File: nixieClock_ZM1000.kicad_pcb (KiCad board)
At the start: 2 copper layers, 124.5 x 88.5 mm, 66 parts, among them J1 Conn_01x08_Female, J2 Conn_01x02_Female, Q1 BC547, Q2 BC547, Q3 BC547, Q4 BC547, Q5 BC547, Q6 BC547, Q7 Q_NMOS_GDS, T1 Transformer_1P_1S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

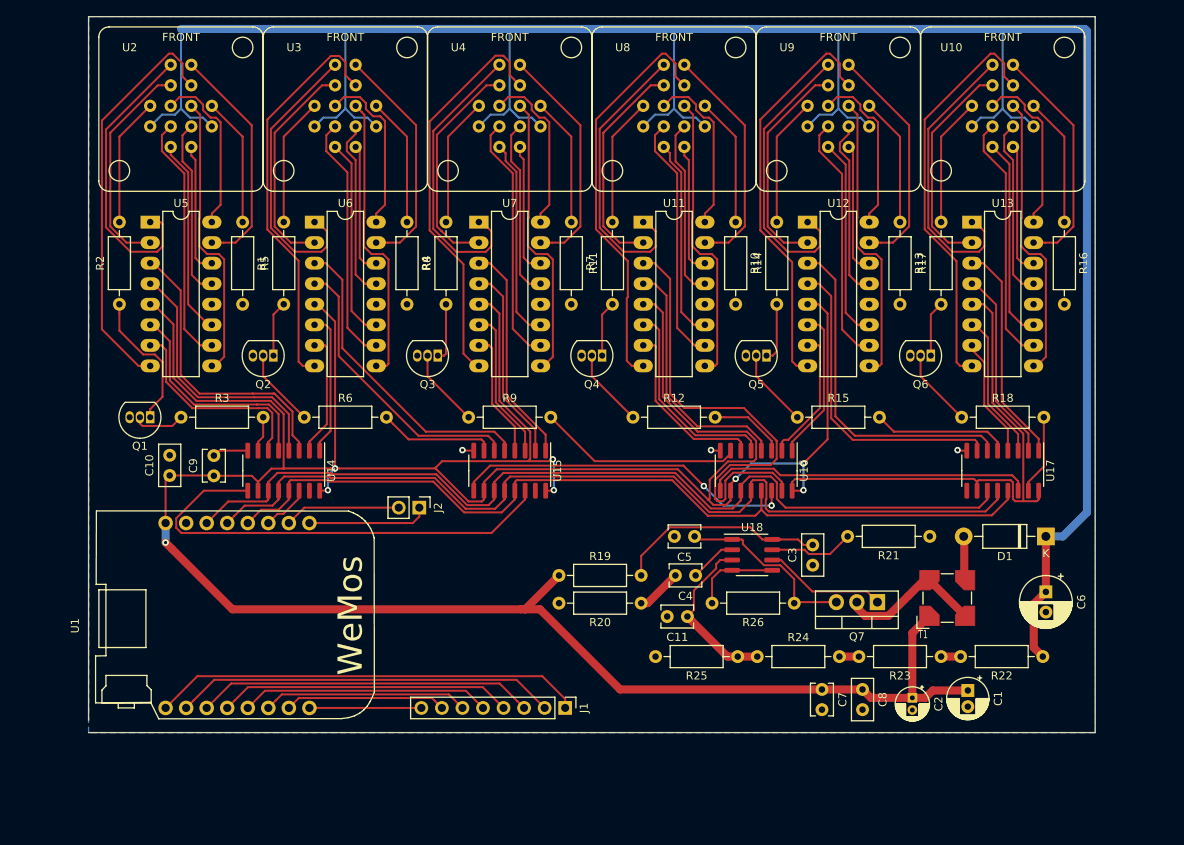
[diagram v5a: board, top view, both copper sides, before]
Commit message: Szitched to DIP shift registers, added BME280
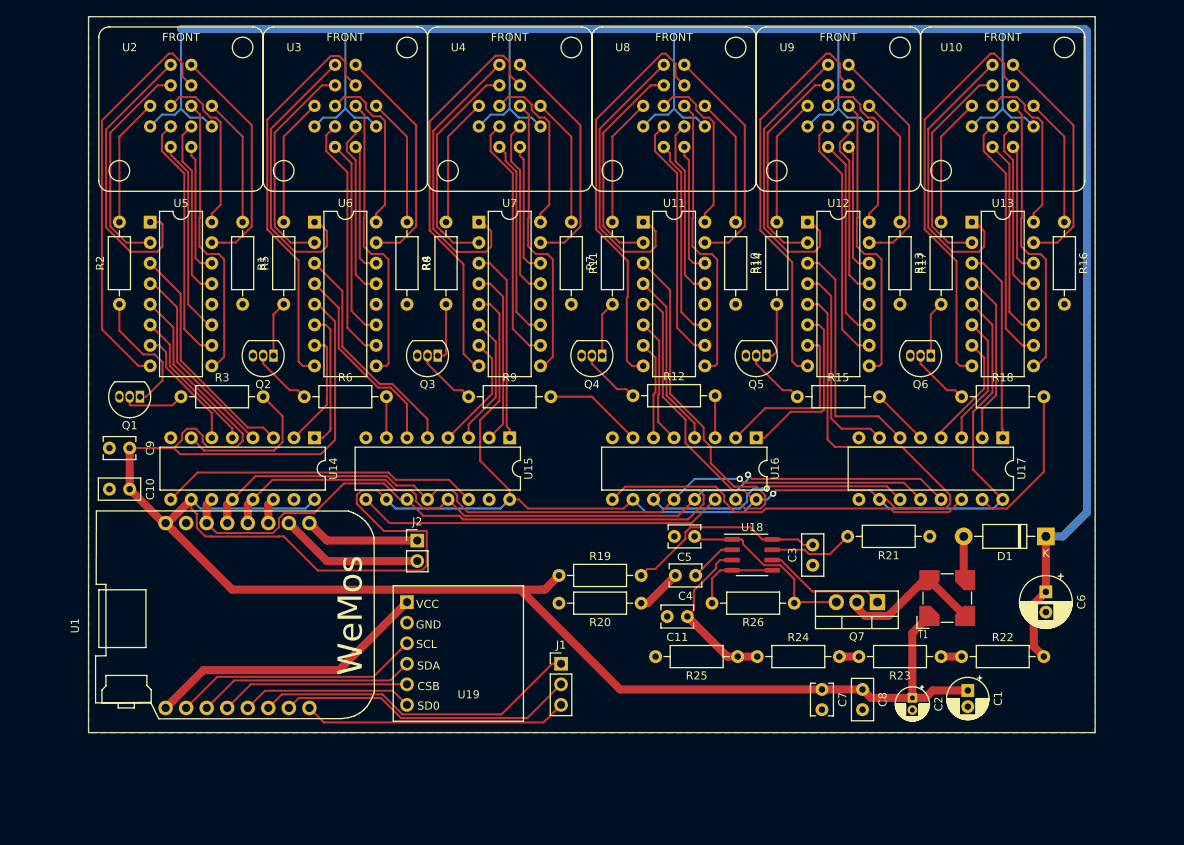
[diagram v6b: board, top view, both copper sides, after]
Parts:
- added U19: BME280, nixies:BME280, F.Cu at (123.2, 125.7)
- J1: value Conn_01x08_Female -> Conn_01x03_Female; footprint Connector_PinHeader_2.54mm:PinHeader_1x08_P2.54mm_Vertical -> Connector_PinHeader_2.54mm:PinHeader_1x03_P2.54mm_Vertical
- U11, U12, U13, U5, U6, U7: footprint Package_DIP:DIP-16_W7.62mm_LongPads -> Package_DIP:DIP-16_W7.62mm
- U14, U15, U16, U17: footprint Package_SO:SOIC-16_3.9x9.9mm_P1.27mm -> Package_DIP:DIP-16_W7.62mm
- moved C9 11.0 mm to (82.5, 100.3), turned to 180 degrees
- moved R22 10.0 mm to (185.4, 126.1), turned to 0 degrees
- moved U14 5.57 mm to (105.4, 99.1)
- moved J1 5.48 mm to (135.9, 127.0), turned to 0 degrees
- moved C10 5.23 mm to (82.5, 105.4), turned to 180 degrees
- moved J2 4.07 mm to (118.1, 111.8), turned to 0 degrees
- moved U15 4.06 mm to (129.5, 99.1)
- moved U16 4.06 mm to (160.0, 99.1)
- moved U17 4.06 mm to (190.5, 99.1)
- moved Q1 2.84 mm to (83.8, 94.0)
- moved R12 2.67 mm to (144.8, 93.9)
- moved R15 2.54 mm to (165.1, 94.0)
- moved R18 2.54 mm to (185.4, 94.0)
- moved R3 2.54 mm to (88.9, 94.0)
- moved R6 2.54 mm to (104.1, 94.0)
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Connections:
- U1 pad 10: Net-(J1-Pad7) -> Net-(J1-Pad2)
- U1 pad 11: Net-(J1-Pad6) -> Net-(J1-Pad1)
- U1 pad 12: Net-(J1-Pad5) -> Net-(U1-Pad12)
- U1 pad 13: Net-(J1-Pad4) -> Net-(U1-Pad13)
- U1 pad 14: Net-(J1-Pad3) -> Net-(U1-Pad14)
- U1 pad 15: Net-(J1-Pad2) -> Net-(U1-Pad15)
- U1 pad 16: Net-(J1-Pad1) -> Net-(U1-Pad16)
- U1 pad 9: Net-(J1-Pad8) -> Net-(J1-Pad3)
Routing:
- net /Control/5V: track 456.2 -> 505.5 mm, vias 8 -> 1
- net Net-(J1-Pad4): track 36.3 -> 0.00 mm
- net Net-(U1-Pad16): track 0.00 -> 35.3 mm
- net Net-(J1-Pad5): track 30.8 -> 0.00 mm
- net Net-(U1-Pad15): track 0.00 -> 30.6 mm
- net Net-(U1-Pad14): track 0.00 -> 27.0 mm
- net Net-(J1-Pad6): track 25.4 -> 0.00 mm
- net Net-(U1-Pad13): track 0.00 -> 23.4 mm
- net Net-(U1-Pad12): track 0.00 -> 21.3 mm
- net Net-(J1-Pad7): track 19.9 -> 0.00 mm
- net /Control/STORAGECLK: track 113.5 -> 95.5 mm, vias 0 -> 1
- net Net-(U14-Pad9): track 57.6 -> 39.6 mm
- net /Shift Registers/BCD_T4A: track 59.9 -> 42.0 mm
- net /Shift Registers/DP1: track 4.39 -> 19.0 mm
- net Net-(J1-Pad8): track 13.8 -> 0.00 mm
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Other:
- outline, holes or cut-outs redrawn

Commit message: Final pending check
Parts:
- added REF**: MountingHole_3.2mm_M3_Pad, MountingHole:MountingHole_3.2mm_M3_Pad, F.Cu at (73.7, 130.8)
- added REF**: MountingHole_3.2mm_M3_Pad, MountingHole:MountingHole_3.2mm_M3_Pad, F.Cu at (205.7, 130.8)
- added REF**: MountingHole_3.2mm_M3_Pad, MountingHole:MountingHole_3.2mm_M3_Pad, F.Cu at (73.7, 52.1)
- added REF**: MountingHole_3.2mm_M3_Pad, MountingHole:MountingHole_3.2mm_M3_Pad, F.Cu at (205.7, 52.1)
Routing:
- net /PSU/HV: track 309.7 -> 333.3 mm
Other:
- board size 124.5 x 88.5 mm -> 142.2 x 88.5 mm
